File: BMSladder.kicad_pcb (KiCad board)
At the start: 2 copper layers, 49.2 x 13 mm, 30 parts, among them J1 Solder in Crimp, J2 Solder in Crimp, J3 HY2.0 Male, J4 Pad TH 1mm, J5 UPDI Port, J6 HY2.0 Male, J7 Solder in Crimp, Q1 MMDT3946, Q2 SI3402-TP, Q3 MMBT3904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

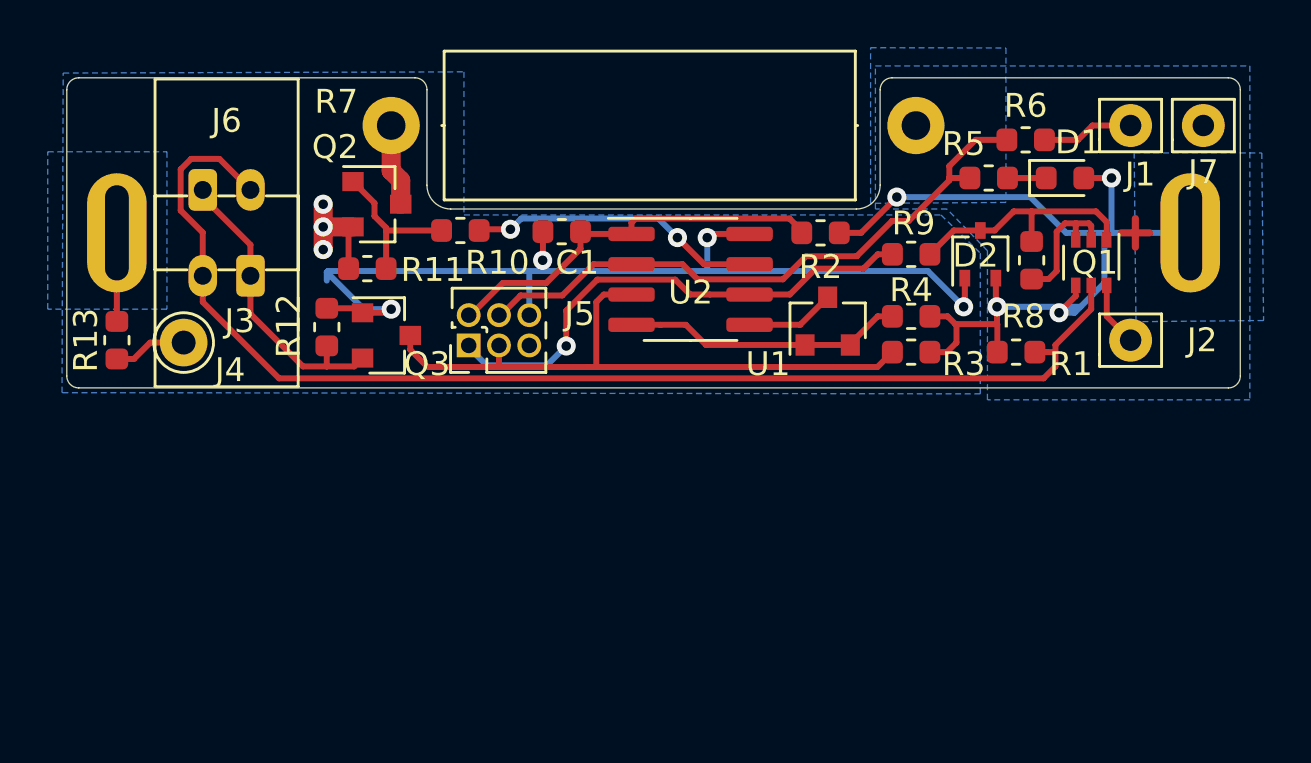
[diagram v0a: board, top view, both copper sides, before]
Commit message: old changes kept just in case
not sure why
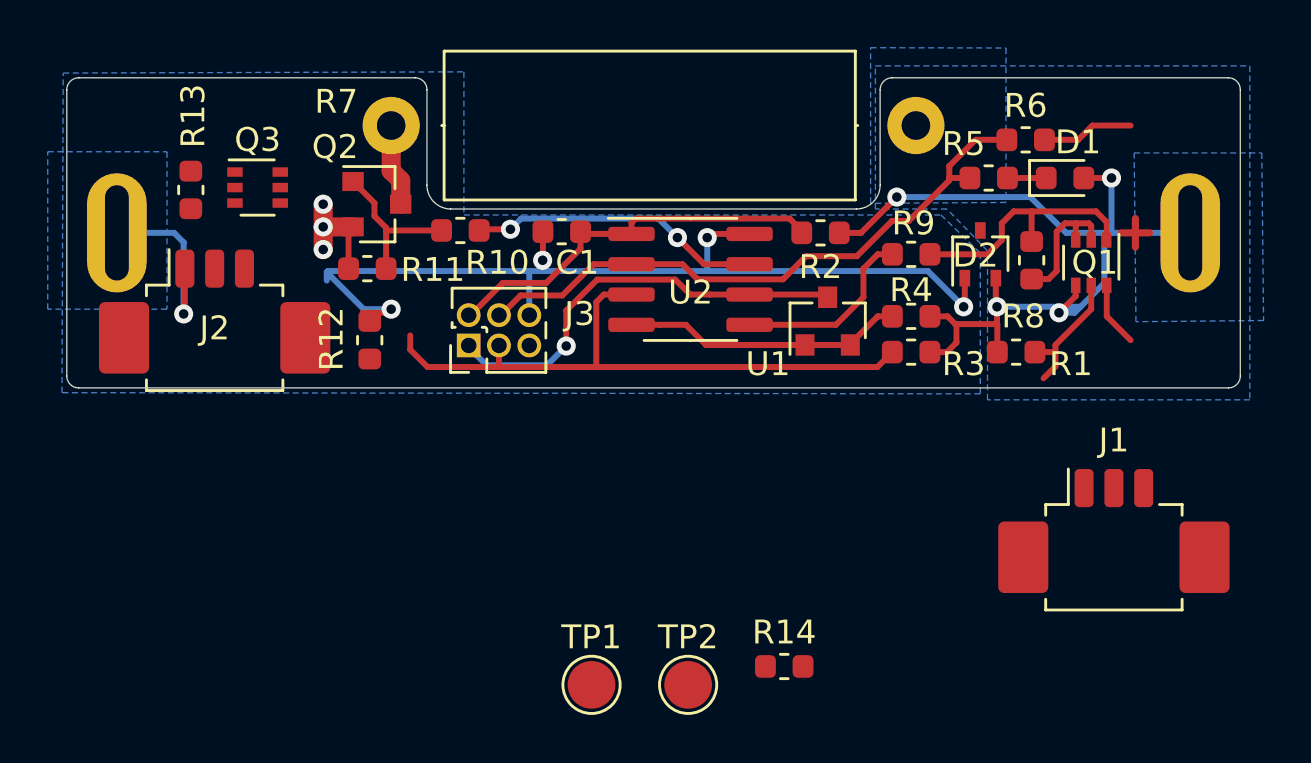
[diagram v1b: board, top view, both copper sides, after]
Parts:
- removed the J3 at (27.6, 27.8)
- removed J4: Pad TH 1mm, Connector_Pin:Pin_D1.0mm_L10.0mm
- removed J6: HY2.0 Male, EdsKicadLibrary:HY2.0mm2P_Header_Horizontal
- removed J7: Solder in Crimp, Connector_Pin:Pin_D0.9mm_L10.0mm_W2.4mm_FlatFork
- added R14: 3K3, Resistor_SMD:R_0603_1608Metric, F.Cu at (50.0, 44.2)
- added TP1: TestPoint, TestPoint:TestPoint_Pad_D2.0mm, F.Cu at (41.9, 45.0)
- added TP2: TestPoint, TestPoint:TestPoint_Pad_D2.0mm, F.Cu at (46.0, 45.0)
- J1, J2: value Solder in Crimp -> HX12501-3AWB; footprint Connector_Pin:Pin_D0.9mm_L10.0mm_W2.4mm_FlatFork -> Connector_Molex:Molex_PicoBlade_53261-0371_1x03-1MP_P1.25mm_Horizontal
- Q3: value MMBT3904 -> MMDT3946; footprint Package_TO_SOT_SMD:SOT-23 -> Package_TO_SOT_SMD:SOT-363_SC-70-6
- R13: value 270k -> 3K3
- moved J2 38.4 mm to (26.1, 29.9)
- moved J1 17.6 mm to (63.8, 39.1)
- moved Q3 8.22 mm to (27.9, 24.1)
- moved R13 7.02 mm to (25.1, 24.2), turned to 90 degrees
- moved R12 1.88 mm to (32.6, 30.5)
- renumbered J5 to J3
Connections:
- D2 pad 1: GND -> Net-(D2-Pad1)
- D2 pad 2: Net-(D1-Pad2) -> Net-(D2-Pad2)
- D2 pad 3: Net-(D2-Pad3) -> Net-(D1-Pad2)
- J1 pad 1: Net-(J1-Pad1) -> Net-(D1-Pad2)
- J2 pad 1: Net-(J2-Pad1) -> GND
- J3 pad 1: /FAULT_UPDI -> /~REFEN~_UPDI
- J3 pad 5: Net-(J5-Pad5) -> (no net)
- Q1 pad 1: Net-(D2-Pad3) -> Net-(Q1-Pad1)
- Q1 pad 5: Net-(J3-Pad2) -> Net-(D2-Pad1)
- Q1 pad 6: Net-(J2-Pad1) -> Net-(D2-Pad2)
- Q3 pad 1: GND -> Net-(Q3-Pad1)
- Q3 pad 2: Net-(J3-Pad1) -> GND
- Q3 pad 3: /RX -> GND
- R1 pad 1: Net-(J3-Pad2) -> Net-(D2-Pad1)
- R12 pad 1: Net-(J3-Pad1) -> Net-(Q3-Pad1)
- R13 pad 1: GND -> Net-(J2-Pad2)
- R13 pad 2: Net-(J4-Pad1) -> Net-(Q3-Pad1)
- R6 pad 2: Net-(J1-Pad1) -> Net-(J1-Pad2)
- R8 pad 1: Net-(D2-Pad3) -> Net-(Q1-Pad1)
- R9 pad 1: Net-(D2-Pad3) -> Net-(Q1-Pad1)
- R9 pad 2: /FAULT_UPDI -> /FAULT
- U1 pad 3: /~EN -> /~REFEN~_UPDI
- U2 pad 5: /~EN -> /FAULT
- U2 pad 6: /FAULT_UPDI -> /~REFEN~_UPDI
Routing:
- net Net-(J3-Pad2): track 51.8 -> 0.00 mm
- net /FAULT_UPDI: track 21.4 -> 0.00 mm, vias 1 -> 0
- net /~REFEN~_UPDI: track 0.00 -> 18.0 mm, vias 0 -> 1
- net Net-(J3-Pad1): track 12.6 -> 0.00 mm
- net Net-(Q1-Pad1): track 0.00 -> 10.8 mm
- net Net-(D2-Pad3): track 10.4 -> 0.00 mm
- net /FAULT: track 0.00 -> 7.91 mm
- net Net-(D2-Pad1): track 0.00 -> 5.59 mm
- net Net-(J1-Pad2): track 0.00 -> 3.88 mm
- net Net-(J1-Pad1): track 3.88 -> 0.00 mm
- net /~EN: track 3.75 -> 0.00 mm
- net Net-(J4-Pad1): track 3.08 -> 0.00 mm
- net Net-(J2-Pad1): track 2.71 -> 0.00 mm
- net Net-(D2-Pad2): track 0.00 -> 2.71 mm
- net GND: track 50.6 -> 53.2 mm, vias 7 -> 8

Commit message: 2023 version
Links now sockets on both ends, cable has two plugs. Swapped pins to make voltage reference programming pin
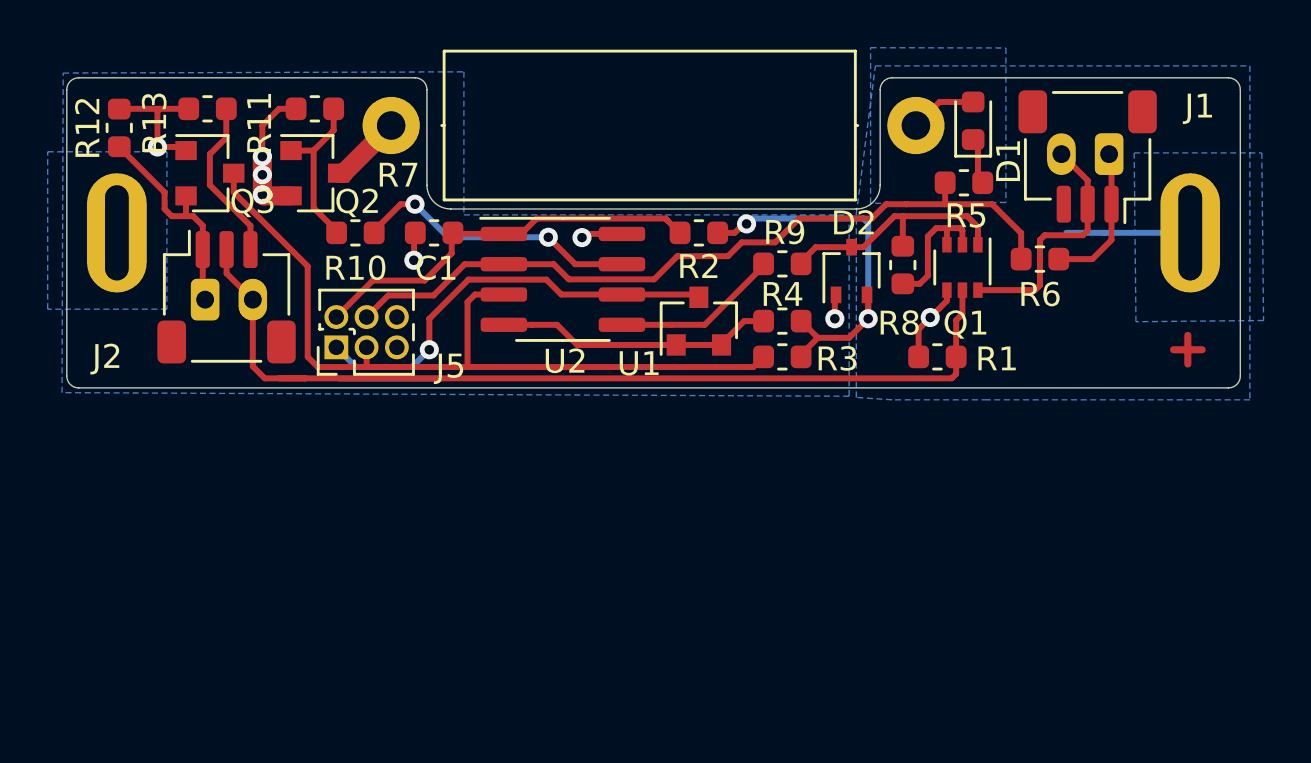
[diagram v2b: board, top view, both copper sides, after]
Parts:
- removed R14: 3K3, Resistor_SMD:R_0603_1608Metric
- removed TP1, TP2: TestPoint, TestPoint:TestPoint_Pad_D2.0mm
- added J3: Conn_01x02, EdsKicadLibrary:HY2.0mm2P_Header_Horizontal, B.Cu at (63.6, 22.7)
- added J4: Conn_01x02, EdsKicadLibrary:HY2.0mm2P_Header_Horizontal, B.Cu at (25.7, 28.8)
- J1, J2: value HX12501-3AWB -> Conn_01x03; footprint Connector_Molex:Molex_PicoBlade_53261-0371_1x03-1MP_P1.25mm_Horizontal -> Connector_JST:JST_SH_SM03B-SRSS-TB_1x03-1MP_P1.00mm_Horizontal
- Q3: value MMDT3946 -> MMBT3904; footprint Package_TO_SOT_SMD:SOT-363_SC-70-6 -> Package_TO_SOT_SMD:SOT-23
- R13: value 3K3 -> 270k
- moved J1 16.3 mm to (62.7, 22.8), turned to 180 degrees
- moved R12 13.8 mm to (22.1, 21.6)
- moved R11 7.05 mm to (30.3, 20.8)
- moved J5 5.55 mm to (31.2, 30.8)
- moved D2 5.45 mm to (52.8, 27.6)
- moved R9 5.41 mm to (49.9, 27.3)
- moved Q1 5.40 mm to (57.5, 27.4)
- moved R3 5.40 mm to (49.9, 31.2)
- moved R4 5.40 mm to (49.9, 29.7)
- moved R8 5.40 mm to (55.0, 27.4)
- moved U1 5.40 mm to (46.4, 29.7)
- moved C1 5.35 mm to (35.3, 26.0)
- moved U2 5.35 mm to (40.7, 27.9)
- moved R2 5.10 mm to (46.4, 26.0)
- moved R6 5.04 mm to (60.7, 27.1)
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- renumbered J3 to J5
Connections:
- net /FAULT renamed /~EN
- net /~REFEN~_UPDI renamed /FAULT_UPDI
- D2 pad 1: Net-(D2-Pad1) -> GND
- D2 pad 2: Net-(D2-Pad2) -> Net-(D1-Pad2)
- D2 pad 3: Net-(D1-Pad2) -> Net-(D2-Pad3)
- J1 pad 1: Net-(D1-Pad2) -> Net-(J1-Pad1)
- J1 pad 3: Net-(D2-Pad2) -> (no net)
- J2 pad 1: GND -> Net-(J2-Pad1)
- Q1 pad 1: Net-(Q1-Pad1) -> Net-(D2-Pad3)
- Q1 pad 5: Net-(D2-Pad1) -> Net-(J2-Pad2)
- Q1 pad 6: Net-(D2-Pad2) -> Net-(J1-Pad2)
- Q3 pad 1: Net-(Q3-Pad1) -> GND
- Q3 pad 2: GND -> Net-(J2-Pad1)
- Q3 pad 3: GND -> /RX
- R1 pad 1: Net-(D2-Pad1) -> Net-(J2-Pad2)
- R12 pad 1: Net-(Q3-Pad1) -> Net-(J2-Pad1)
- R13 pad 1: Net-(J2-Pad2) -> GND
- R13 pad 2: Net-(Q3-Pad1) -> Net-(J2-Pad3)
- R6 pad 2: Net-(J1-Pad2) -> Net-(J1-Pad1)
- R8 pad 1: Net-(Q1-Pad1) -> Net-(D2-Pad3)
- R9 pad 1: Net-(Q1-Pad1) -> Net-(D2-Pad3)
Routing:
- net Net-(J2-Pad2): track 0.00 -> 39.8 mm
- net GND: track 53.2 -> 20.5 mm, vias 8 -> 7
- net /RX: track 26.8 -> 39.2 mm
- net Net-(Q1-Pad1): track 10.8 -> 0.00 mm
- net Net-(D2-Pad3): track 0.00 -> 10.5 mm
- net Net-(D1-Pad2): track 37.3 -> 27.8 mm, vias 4 -> 3
- net Net-(J2-Pad1): track 0.00 -> 9.28 mm
- net Net-(J2-Pad3): track 0.00 -> 6.89 mm
- net Net-(J1-Pad2): track 3.88 -> 10.4 mm
- net /TX: track 26.1 -> 32.4 mm
- net Net-(J1-Pad1): track 0.00 -> 6.19 mm
- net Net-(D2-Pad1): track 5.59 -> 0.00 mm
- net Net-(D2-Pad2): track 2.71 -> 0.00 mm
- net /VCC: track 16.7 -> 17.6 mm
- net /~EN: track 7.91 -> 7.10 mm
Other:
- rule trace_min: 0.2 -> 0.25
- board text added: "BMS LADDER RUNG 1 CELL ALARM PCB REV 1.1 (c) 2023 EHC"
- board text removed: "1 CELL ALARM PCB (c) 2021 EHC"
